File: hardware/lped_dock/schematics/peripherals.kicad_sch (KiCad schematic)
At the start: 4 parts, among them SW1 Pair button

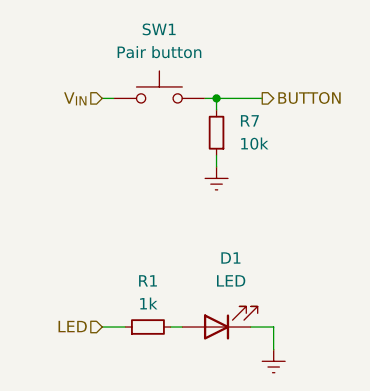
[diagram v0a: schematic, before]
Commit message: feat(hardware): remove unused parts from dock pcb
* Removed LED from dock
* Removed button from dock
* Removed connection pins for LED and button
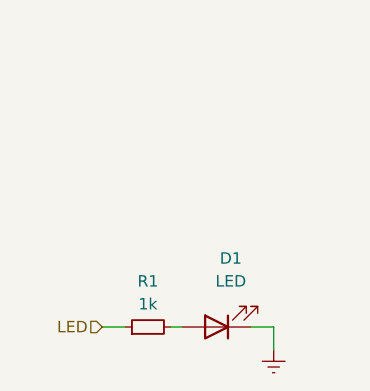
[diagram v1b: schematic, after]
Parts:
- removed R7: 10k, Resistor_SMD:R_0402_1005Metric, symbol Device:R_Small
- removed SW1: Pair button, Button_Switch_SMD:SW_SPST_PTS645, symbol Switch:SW_Push
